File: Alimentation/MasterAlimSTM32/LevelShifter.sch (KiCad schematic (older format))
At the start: 3 parts, among them Q1 BSS138

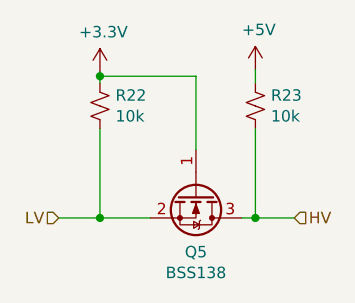
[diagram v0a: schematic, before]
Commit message: Module alim ISO, clean master alim
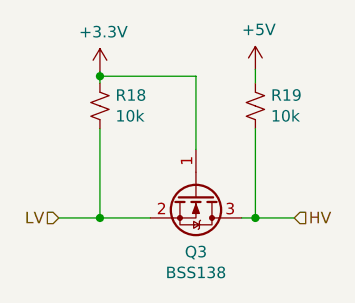
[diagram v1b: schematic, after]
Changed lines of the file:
@@
 $Descr A4 11693 8268
 encoding utf-8
-Sheet 6 13
+Sheet 4 13
 Title ""
 Date ""
@@
 AR Path="/60B1A7AD/60A5C33B" Ref="#PWR0157"  Part="1"
 AR Path="/60B1A7B2/60A5C33B" Ref="#PWR0159"  Part="1"
-F 0 "#PWR0157" H 5850 4650 50  0001 C CNN
+F 0 "#PWR0153" H 5850 4650 50  0001 C CNN
 F 1 "+3.3V" H 5865 4973 50  0000 C CNN
 F 2 "" H 5850 4800 50  0001 C CNN
 F 3 "" H 5850 4800 50  0001 C CNN
 	1    5850 4800
-	1    0    0    -1
-$EndComp
-$Comp
-L power:+5V #PWR0150
-U 1 1 60A5C83D
-P 6530 4790
-AR Path="/60A5B5F2/60A5C83D" Ref="#PWR0150"  Part="1"
-AR Path="/60AC988E/60A5C83D" Ref="#PWR0152"  Part="1"
-AR Path="/60B0E1DC/60A5C83D" Ref="#PWR0154"  Part="1"
-AR Path="/60B0E1E1/60A5C83D" Ref="#PWR0156"  Part="1"
-AR Path="/60B1A7AD/60A5C83D" Ref="#PWR0158"  Part="1"
-AR Path="/60B1A7B2/60A5C83D" Ref="#PWR0160"  Part="1"
-F 0 "#PWR0158" H 6530 4640 50  0001 C CNN
-F 1 "+5V" H 6545 4963 50  0000 C CNN
-F 2 "" H 6530 4790 50  0001 C CNN
-F 3 "" H 6530 4790 50  0001 C CNN
-	1    6530 4790
-	1    0    0    -1
-$EndComp
-$Comp
-L Transistor_FET:BSS138 Q1
-U 1 1 60A5CFB1
-P 6270 5340
-AR Path="/60A5B5F2/60A5CFB1" Ref="Q1"  Part="1"
-AR Path="/60AC988E/60A5CFB1" Ref="Q2"  Part="1"
-AR Path="/60B0E1DC/60A5CFB1" Ref="Q3"  Part="1"
-AR Path="/60B0E1E1/60A5CFB1" Ref="Q4"  Part="1"
-AR Path="/60B1A7AD/60A5CFB1" Ref="Q5"  Part="1"
-AR Path="/60B1A7B2/60A5CFB1" Ref="Q6"  Part="1"
-F 0 "Q5" V 6519 5340 50  0000 C CNN
-F 1 "BSS138" V 6610 5340 50  0000 C CNN
-F 2 "Package_TO_SOT_SMD:SOT-23" H 6470 5265 50  0001 L CIN
-F 3 "https://www.onsemi.com/pub/Collateral/BSS138-D.PDF" H 6270 5340 50  0001 L CNN
-	1    6270 5340
-	0    1    1    0
-$EndComp
-$Comp
-L Device:R_Small_US R15
-U 1 1 60A618C8
-P 6530 4950
-AR Path="/60A5B5F2/60A618C8" Ref="R15"  Part="1"
-AR Path="/60AC988E/60A618C8" Ref="R17"  Part="1"
-AR Path="/60B0E1DC/60A618C8" Ref="R19"  Part="1"
-AR Path="/60B0E1E1/60A618C8" Ref="R21"  Part="1"
-AR Path="/60B1A7AD/60A618C8" Ref="R23"  Part="1"
-AR Path="/60B1A7B2/60A618C8" Ref="R25"  Part="1"
-F 0 "R23" H 6598 4996 50  0000 L CNN
-F 1 "10k" H 6598 4905 50  0000 L CNN
-F 2 "" H 6530 4950 50  0001 C CNN
-F 3 "~" H 6530 4950 50  0001 C CNN
-	1    6530 4950
 	1    0    0    -1
 $EndComp
@@
 AR Path="/60B1A7AD/60A62254" Ref="R22"  Part="1"
 AR Path="/60B1A7B2/60A62254" Ref="R24"  Part="1"
-F 0 "R22" H 5918 4996 50  0000 L CNN
+F 0 "R18" H 5918 4996 50  0000 L CNN
 F 1 "10k" H 5918 4905 50  0000 L CNN
 F 2 "" H 5850 4950 50  0001 C CNN
@@
 Connection ~ 5850 4820
 Wire Wire Line
-	6530 4790 6530 4850
-Wire Wire Line
-	6470 5440 6530 5440
-Wire Wire Line
-	6530 5440 6530 5050
-Wire Wire Line
-	6530 5440 6700 5440
-Connection ~ 6530 5440
-Wire Wire Line
 	5850 5440 5670 5440
 Connection ~ 5850 5440
@@
 Text HLabel 5670 5440 0    50   Input ~ 0
 LV
+Connection ~ 6530 5440
+Wire Wire Line
+	6530 5440 6700 5440
+Wire Wire Line
+	6470 5440 6530 5440
+Wire Wire Line
+	6530 5440 6530 5050
+Wire Wire Line
+	6530 4790 6530 4850
+$Comp
+L Transistor_FET:BSS138 Q1
+U 1 1 60A5CFB1
+P 6270 5340
+AR Path="/60A5B5F2/60A5CFB1" Ref="Q1"  Part="1"
+AR Path="/60AC988E/60A5CFB1" Ref="Q2"  Part="1"
+AR Path="/60B0E1DC/60A5CFB1" Ref="Q3"  Part="1"
+AR Path="/60B0E1E1/60A5CFB1" Ref="Q4"  Part="1"
+AR Path="/60B1A7AD/60A5CFB1" Ref="Q5"  Part="1"
+AR Path="/60B1A7B2/60A5CFB1" Ref="Q6"  Part="1"
+F 0 "Q3" V 6519 5340 50  0000 C CNN
+F 1 "BSS138" V 6610 5340 50  0000 C CNN
+F 2 "Package_TO_SOT_SMD:SOT-23" H 6470 5265 50  0001 L CIN
+F 3 "https://www.onsemi.com/pub/Collateral/BSS138-D.PDF" H 6270 5340 50  0001 L CNN
+	1    6270 5340
+	0    1    1    0
+$EndComp
+$Comp
+L power:+5V #PWR0150
+U 1 1 60A5C83D
+P 6530 4790
+AR Path="/60A5B5F2/60A5C83D" Ref="#PWR0150"  Part="1"
+AR Path="/60AC988E/60A5C83D" Ref="#PWR0152"  Part="1"
+AR Path="/60B0E1DC/60A5C83D" Ref="#PWR0154"  Part="1"
+AR Path="/60B0E1E1/60A5C83D" Ref="#PWR0156"  Part="1"
+AR Path="/60B1A7AD/60A5C83D" Ref="#PWR0158"  Part="1"
+AR Path="/60B1A7B2/60A5C83D" Ref="#PWR0160"  Part="1"
+F 0 "#PWR0154" H 6530 4640 50  0001 C CNN
+F 1 "+5V" H 6545 4963 50  0000 C CNN
+F 2 "" H 6530 4790 50  0001 C CNN
+F 3 "" H 6530 4790 50  0001 C CNN
+	1    6530 4790
+	1    0    0    -1
+$EndComp
+$Comp
+L Device:R_Small_US R15
+U 1 1 60A618C8
+P 6530 4950
+AR Path="/60A5B5F2/60A618C8" Ref="R15"  Part="1"
+AR Path="/60AC988E/60A618C8" Ref="R17"  Part="1"
+AR Path="/60B0E1DC/60A618C8" Ref="R19"  Part="1"
+AR Path="/60B0E1E1/60A618C8" Ref="R21"  Part="1"
+AR Path="/60B1A7AD/60A618C8" Ref="R23"  Part="1"
+AR Path="/60B1A7B2/60A618C8" Ref="R25"  Part="1"
+F 0 "R19" H 6598 4996 50  0000 L CNN
+F 1 "10k" H 6598 4905 50  0000 L CNN
+F 2 "" H 6530 4950 50  0001 C CNN
+F 3 "~" H 6530 4950 50  0001 C CNN
+	1    6530 4950
+	1    0    0    -1
+$EndComp
 $EndSCHEMATC
